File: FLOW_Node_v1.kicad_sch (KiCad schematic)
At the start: 37 parts, among them J1 Conn_01x04_Pin, J2 Conn_01x05_Pin, J5 Conn_02x05_Odd_Even, J7 Conn_01x04_Pin, J8 Conn_01x02, J9 Conn_01x02, U1 STM32L053R8Tx, U2 MAX7375AXR805

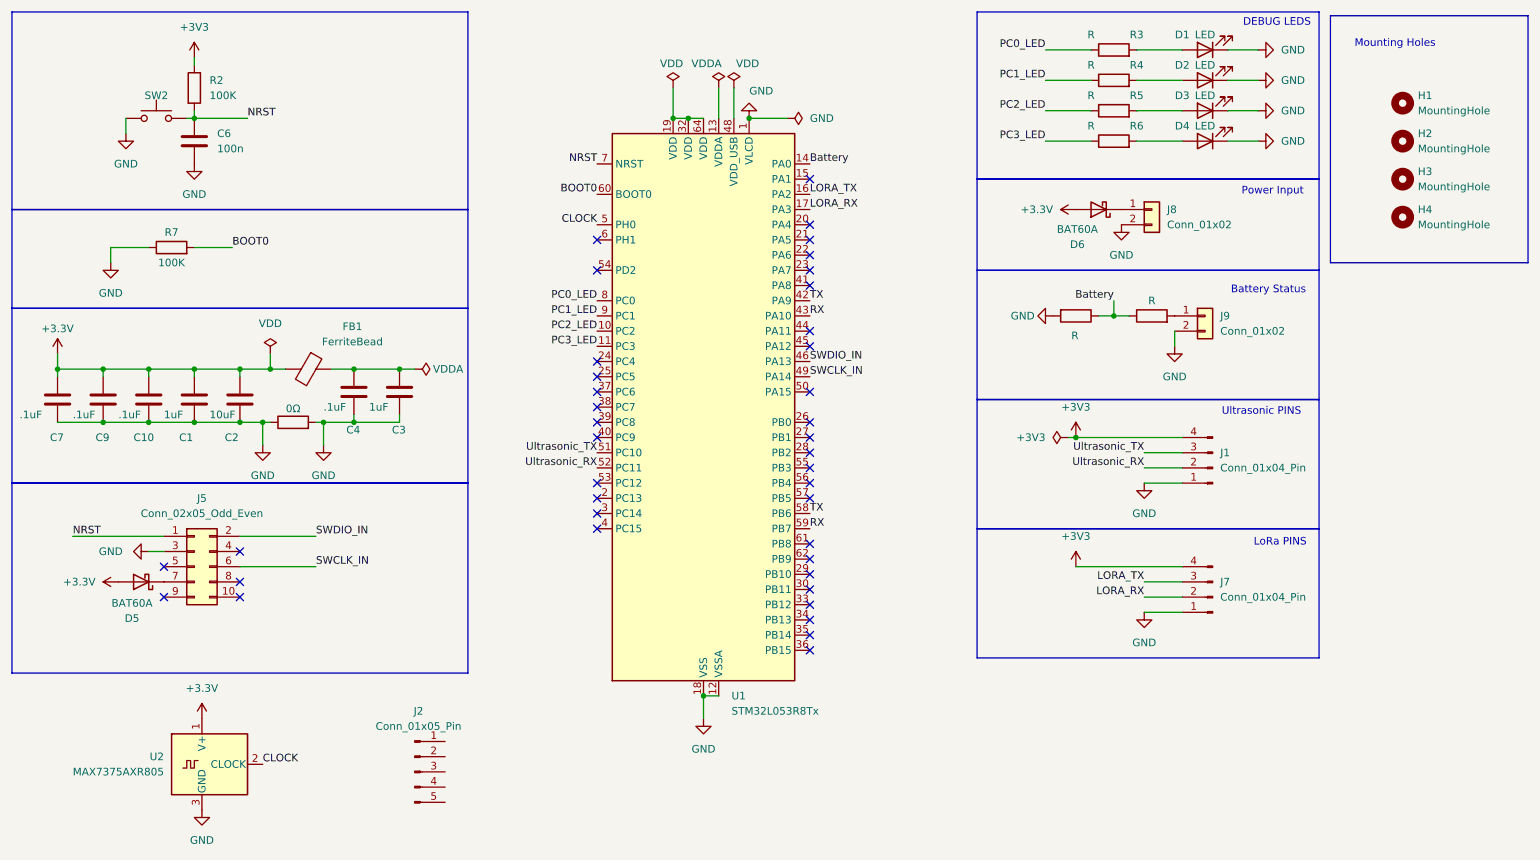
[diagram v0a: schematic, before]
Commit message: Newest Node PCB
with ground plane
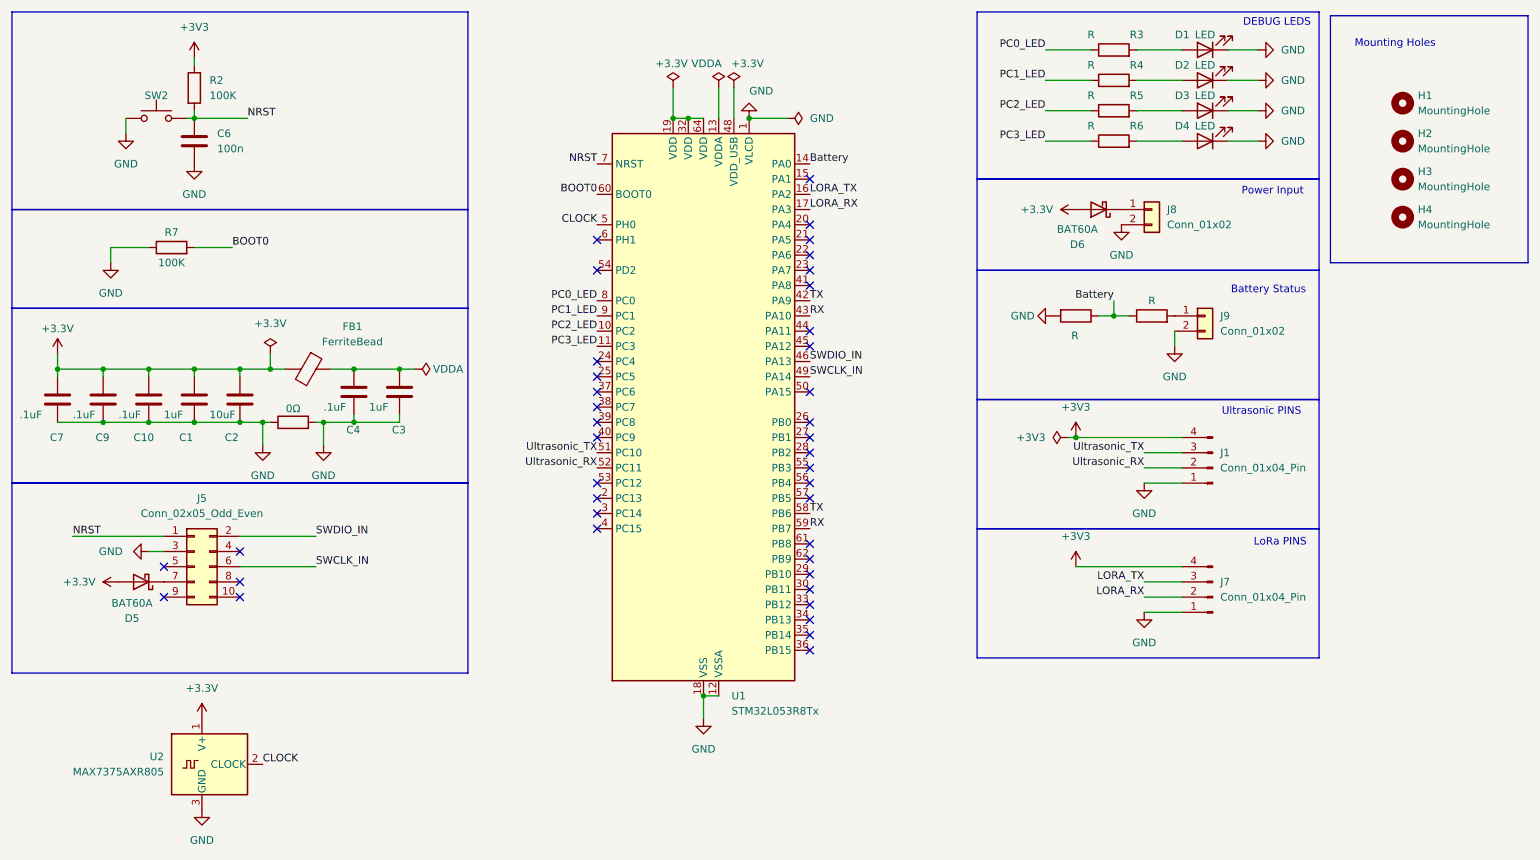
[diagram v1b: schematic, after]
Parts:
- removed J2: Conn_01x05_Pin, symbol Connector:Conn_01x05_Pin
- J5: footprint Connector_PinHeader_2.54mm:PinHeader_1x05_P2.54mm_Vertical -> Connector_PinHeader_2.54mm:PinHeader_2x05_P2.54mm_Vertical
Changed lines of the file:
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@@
 			)
 		)
-		(property "Value" "VDD"
+		(property "Value" "+3.3V"
 			(at 122.936 21.336 0)
 			(effects
@@
 			)
 		)
-		(property "Value" "VDD"
+		(property "Value" "+3.3V"
 			(at 135.636 21.336 0)
 			(effects
@@
 	)
 	(symbol
-		(lib_id "Connector:Conn_01x05_Pin")
-		(at 80.01 139.7 0)
-		(unit 1)
-		(exclude_from_sim no)
-		(in_bom yes)
-		(on_board yes)
-		(dnp no)
-		(fields_autoplaced yes)
-		(property "Reference" "J2"
-			(at 80.645 129.54 0)
-			(effects
-				(font
-					(size 1.27 1.27)
-				)
-			)
-		)
-		(property "Value" "Conn_01x05_Pin"
-			(at 80.645 132.08 0)
-			(effects
-				(font
-					(size 1.27 1.27)
-				)
-			)
-		)
-		(property "Footprint" ""
-			(at 80.01 139.7 0)
-			(effects
-				(font
-					(size 1.27 1.27)
-				)
-				(hide yes)
-			)
-		)
-		(property "Datasheet" "~"
-			(at 80.01 139.7 0)
-			(effects
-				(font
-					(size 1.27 1.27)
-				)
-				(hide yes)
-			)
-		)
-		(property "Description" "Generic connector, single row, 01x05, script generated"
-			(at 80.01 139.7 0)
-			(effects
-				(font
-					(size 1.27 1.27)
-				)
-				(hide yes)
-			)
-		)
-		(pin "4"
-		)
-		(pin "1"
-		)
-		(pin "2"
-		)
-		(pin "5"
-		)
-		(pin "3"
-		)
-		(instances
-			(project ""
-				(path "/d3521264-adf0-4a8d-b720-9cc64583c997"
-					(reference "J2")
-					(unit 1)
-				)
-			)
-		)
-	)
-	(symbol
 		(lib_id "power:+3V3")
 		(at 43.18 20.32 0)
@@
 			)
 		)
-		(property "Footprint" "Connector_PinHeader_2.54mm:PinHeader_1x05_P2.54mm_Vertical"
+		(property "Footprint" "Connector_PinHeader_2.54mm:PinHeader_2x05_P2.54mm_Vertical"
 			(at 43.18 105.41 0)
 			(effects
@@
 			)
 		)
-		(property "Value" "VDD"
+		(property "Value" "+3.3V"
 			(at 55.88 64.77 0)
 			(effects
